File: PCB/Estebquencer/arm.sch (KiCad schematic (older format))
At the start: 1 part

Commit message: se cablearon los módulos al ARM, se añadió el conector JTAG (SWD)
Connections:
- net labels added: DAC_#Sync, DAC_Din, DAC_Sclk, DISP_CHAR0, DISP_CHAR1, DISP_CHAR2, DISP_CHAR3, DISP_EN, DISP_SCK, DISP_SER, SWCLK, SWDIO, encoder_L, encoder_R, encoder_click
- wire segments 14 -> 31
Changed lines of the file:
@@
 Connection ~ 5850 1650
 $Sheet
-S 1200 6500 1000 500
+S 1700 6500 500  500
 U 5875F97F
 F0 "JTAG" 197
 F1 "JTAG.sch" 60
+F2 "SWDIO" I R 2200 6700 60
+F3 "SWCLK" I R 2200 6800 60
 $EndSheet
 Text HLabel 2900 4100 0    60   Input ~ 0
@@
 Wire Wire Line
 	2900 4100 3050 4100
+Text GLabel 9050 4800 2    60   Input ~ 0
+SWDIO
+Text GLabel 9050 4900 2    60   Input ~ 0
+SWCLK
+Wire Wire Line
+	9050 4900 8850 4900
+Wire Wire Line
+	8850 4800 9050 4800
+Text GLabel 2300 6700 2    60   Input ~ 0
+SWDIO
+Text GLabel 2300 6800 2    60   Input ~ 0
+SWCLK
+Wire Wire Line
+	2200 6800 2300 6800
+Wire Wire Line
+	2300 6700 2200 6700
+Text HLabel 2900 3100 0    60   Input ~ 0
+encoder_L
+Text HLabel 2900 3200 0    60   Input ~ 0
+encoder_R
+Text HLabel 2900 3300 0    60   Input ~ 0
+encoder_click
+Wire Wire Line
+	2900 3100 3050 3100
+Wire Wire Line
+	3050 3200 2900 3200
+Wire Wire Line
+	2900 3300 3050 3300
+Text HLabel 2900 4000 0    60   Input ~ 0
+DAC_Din
+Text HLabel 2900 3800 0    60   Input ~ 0
+DAC_Sclk
+Text HLabel 2900 3900 0    60   Input ~ 0
+DAC_#Sync
+Wire Wire Line
+	2900 3800 3050 3800
+Wire Wire Line
+	2900 3900 3050 3900
+Wire Wire Line
+	3050 4000 2900 4000
+Text HLabel 2900 4800 0    60   Input ~ 0
+DISP_SCK
+Text HLabel 2900 5000 0    60   Input ~ 0
+DISP_SER
+Text HLabel 2900 4700 0    60   Input ~ 0
+DISP_EN
+Wire Wire Line
+	2900 4700 3050 4700
+Wire Wire Line
+	2900 4800 3050 4800
+Wire Wire Line
+	2900 5000 3050 5000
+Text HLabel 2900 4300 0    60   Input ~ 0
+DISP_CHAR0
+Text HLabel 2900 4400 0    60   Input ~ 0
+DISP_CHAR1
+Text HLabel 2900 4500 0    60   Input ~ 0
+DISP_CHAR2
+Text HLabel 2900 4600 0    60   Input ~ 0
+DISP_CHAR3
+Wire Wire Line
+	2900 4600 3050 4600
+Wire Wire Line
+	3050 4500 2900 4500
+Wire Wire Line
+	2900 4400 3050 4400
+Wire Wire Line
+	3050 4300 2900 4300
 $EndSCHEMATC

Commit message: Añadido proyecto ST, configuración superficial de todos los periféricos, falta crear los threads en FreeRTOS
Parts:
- U?: symbol STM32F103C8T6 -> libreria_proyecto:STM32F103C8T6
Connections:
- net labels added: Btn_C1, Btn_C2, Btn_C3, Btn_C4, Btn_C5, Btn_C6, Btn_C7, Btn_R1, Btn_R2, Btn_R3, CLK_OUT_1, CLK_OUT_2, CLK_in_1, CLK_in_2, DAC1_CS, DAC2_CS, DAC_MISO, DAC_MOSI, DAC_SCK, Debug_Rx, Debug_Tx, LED_R1, LED_R2, LED_R3, LED_R4, LED_R5, LED_R6, LED_R7, USB_D+, USB_D-
- net labels removed: DAC_#Sync, DAC_Din, DAC_Sclk, DISP_CHAR0, DISP_CHAR1, DISP_CHAR2, DISP_CHAR3, DISP_EN, DISP_SCK, DISP_SER, MIDI_RX, MIDI_TX, encoder_L, encoder_R, encoder_click
- wire segments 31 -> 52

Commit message: acabado módulo ARM
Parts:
- added C? (x4): 100nF, symbol Device:C_Small
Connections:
- net GNDREF is gone; now on net GND: U?.23 (VSS), U?.35 (VSS), U?.47 (VSS)
- net +3V3: now also U?.9 (VDDA), C?.1, C?.1, C?.1, C?.1
- net GND: now reaches U?.8 (VSSA)
- net GND: now also C?.2, C?.2, C?.2, C?.2
- no-connect marks 0 -> 3
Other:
- note added: "To ARM"
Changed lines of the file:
@@
 Wire Wire Line
 	1400 6300 1450 6300
-$Comp
-L power:GNDREF #PWR?
-U 1 1 5875F33E
-P 6100 5850
-F 0 "#PWR?" H 6100 5600 50  0001 C CNN
-F 1 "GNDREF" H 6100 5700 50  0000 C CNN
-F 2 "" H 6100 5850 50  0000 C CNN
-F 3 "" H 6100 5850 50  0000 C CNN
-	1    6100 5850
-	1    0    0    -1
-$EndComp
 Wire Wire Line
 	6100 5850 6100 5400
@@
 Wire Wire Line
 	3300 4800 3400 4800
+Wire Wire Line
+	9200 4900 9400 4900
+NoConn ~ 9400 4900
+Wire Wire Line
+	9400 3500 9200 3500
+Wire Wire Line
+	9200 3400 9400 3400
+NoConn ~ 9400 3400
+NoConn ~ 9400 3500
+Connection ~ 6300 5400
+Wire Wire Line
+	6400 5300 6400 5400
+Wire Wire Line
+	6300 5400 6400 5400
+Wire Wire Line
+	6400 1700 6400 1550
+Wire Wire Line
+	6400 1550 6300 1550
+Connection ~ 6300 1550
+$Comp
+L Device:C_Small C?
+U 1 1 5E3C7F8F
+P 3950 7000
+F 0 "C?" H 4000 6850 50  0000 L CNN
+F 1 "100nF" V 4050 6900 50  0000 L CNN
+F 2 "" H 3950 7000 50  0001 C CNN
+F 3 "~" H 3950 7000 50  0001 C CNN
+	1    3950 7000
+	1    0    0    -1
+$EndComp
+$Comp
+L Device:C_Small C?
+U 1 1 5E3C867B
+P 3700 7000
+F 0 "C?" H 3750 6850 50  0000 L CNN
+F 1 "100nF" V 3800 6900 50  0000 L CNN
+F 2 "" H 3700 7000 50  0001 C CNN
+F 3 "~" H 3700 7000 50  0001 C CNN
+	1    3700 7000
+	1    0    0    -1
+$EndComp
+$Comp
+L power:GND #PWR?
+U 1 1 5E3C872F
+P 6100 5850
+F 0 "#PWR?" H 6100 5600 50  0001 C CNN
+F 1 "GND" H 6105 5677 50  0000 C CNN
+F 2 "" H 6100 5850 50  0001 C CNN
+F 3 "" H 6100 5850 50  0001 C CNN
+	1    6100 5850
+	1    0    0    -1
+$EndComp
+$Comp
+L power:GND #PWR?
+U 1 1 5E3CBE0D
+P 3950 7200
+F 0 "#PWR?" H 3950 6950 50  0001 C CNN
+F 1 "GND" H 3955 7027 50  0000 C CNN
+F 2 "" H 3950 7200 50  0001 C CNN
+F 3 "" H 3950 7200 50  0001 C CNN
+	1    3950 7200
+	1    0    0    -1
+$EndComp
+$Comp
+L power:+3.3V #PWR?
+U 1 1 5E3CBE42
+P 3950 6800
+F 0 "#PWR?" H 3950 6650 50  0001 C CNN
+F 1 "+3.3V" H 3950 6940 50  0000 C CNN
+F 2 "" H 3950 6800 50  0000 C CNN
+F 3 "" H 3950 6800 50  0000 C CNN
+	1    3950 6800
+	1    0    0    -1
+$EndComp
+$Comp
+L power:+3.3V #PWR?
+U 1 1 5E3CBE88
+P 3700 6800
+F 0 "#PWR?" H 3700 6650 50  0001 C CNN
+F 1 "+3.3V" H 3700 6940 50  0000 C CNN
+F 2 "" H 3700 6800 50  0000 C CNN
+F 3 "" H 3700 6800 50  0000 C CNN
+	1    3700 6800
+	1    0    0    -1
+$EndComp
+$Comp
+L power:GND #PWR?
+U 1 1 5E3CBEC9
+P 3700 7200
+F 0 "#PWR?" H 3700 6950 50  0001 C CNN
+F 1 "GND" H 3705 7027 50  0000 C CNN
+F 2 "" H 3700 7200 50  0001 C CNN
+F 3 "" H 3700 7200 50  0001 C CNN
+	1    3700 7200
+	1    0    0    -1
+$EndComp
+Wire Wire Line
+	3700 7200 3700 7100
+Wire Wire Line
+	3700 6900 3700 6800
+Wire Wire Line
+	3950 6800 3950 6900
+Wire Wire Line
+	3950 7100 3950 7200
+$Comp
+L Device:C_Small C?
+U 1 1 5E3D0FF3
+P 4700 7000
+F 0 "C?" H 4750 6850 50  0000 L CNN
+F 1 "100nF" V 4800 6900 50  0000 L CNN
+F 2 "" H 4700 7000 50  0001 C CNN
+F 3 "~" H 4700 7000 50  0001 C CNN
+	1    4700 7000
+	1    0    0    -1
+$EndComp
+$Comp
+L Device:C_Small C?
+U 1 1 5E3D0FF9
+P 4450 7000
+F 0 "C?" H 4500 6850 50  0000 L CNN
+F 1 "100nF" V 4550 6900 50  0000 L CNN
+F 2 "" H 4450 7000 50  0001 C CNN
+F 3 "~" H 4450 7000 50  0001 C CNN
+	1    4450 7000
+	1    0    0    -1
+$EndComp
+$Comp
+L power:GND #PWR?
+U 1 1 5E3D0FFF
+P 4700 7200
+F 0 "#PWR?" H 4700 6950 50  0001 C CNN
+F 1 "GND" H 4705 7027 50  0000 C CNN
+F 2 "" H 4700 7200 50  0001 C CNN
+F 3 "" H 4700 7200 50  0001 C CNN
+	1    4700 7200
+	1    0    0    -1
+$EndComp
+$Comp
+L power:+3.3V #PWR?
+U 1 1 5E3D1005
+P 4700 6800
+F 0 "#PWR?" H 4700 6650 50  0001 C CNN
+F 1 "+3.3V" H 4700 6940 50  0000 C CNN
+F 2 "" H 4700 6800 50  0000 C CNN
+F 3 "" H 4700 6800 50  0000 C CNN
+	1    4700 6800
+	1    0    0    -1
+$EndComp
+$Comp
+L power:+3.3V #PWR?
+U 1 1 5E3D100B
+P 4450 6800
+F 0 "#PWR?" H 4450 6650 50  0001 C CNN
+F 1 "+3.3V" H 4450 6940 50  0000 C CNN
+F 2 "" H 4450 6800 50  0000 C CNN
+F 3 "" H 4450 6800 50  0000 C CNN
+	1    4450 6800
+	1    0    0    -1
+$EndComp
+$Comp
+L power:GND #PWR?
+U 1 1 5E3D1011
+P 4450 7200
+F 0 "#PWR?" H 4450 6950 50  0001 C CNN
+F 1 "GND" H 4455 7027 50  0000 C CNN
+F 2 "" H 4450 7200 50  0001 C CNN
+F 3 "" H 4450 7200 50  0001 C CNN
+	1    4450 7200
+	1    0    0    -1
+$EndComp
+Wire Wire Line
+	4450 7200 4450 7100
+Wire Wire Line
+	4450 6900 4450 6800
+Wire Wire Line
+	4700 6800 4700 6900
+Wire Wire Line
+	4700 7100 4700 7200
+Text Notes 3700 6500 0    60   ~ 0
+To ARM
+Text Notes 4450 6500 0    60   ~ 0
+To ARM
 $EndSCHEMATC

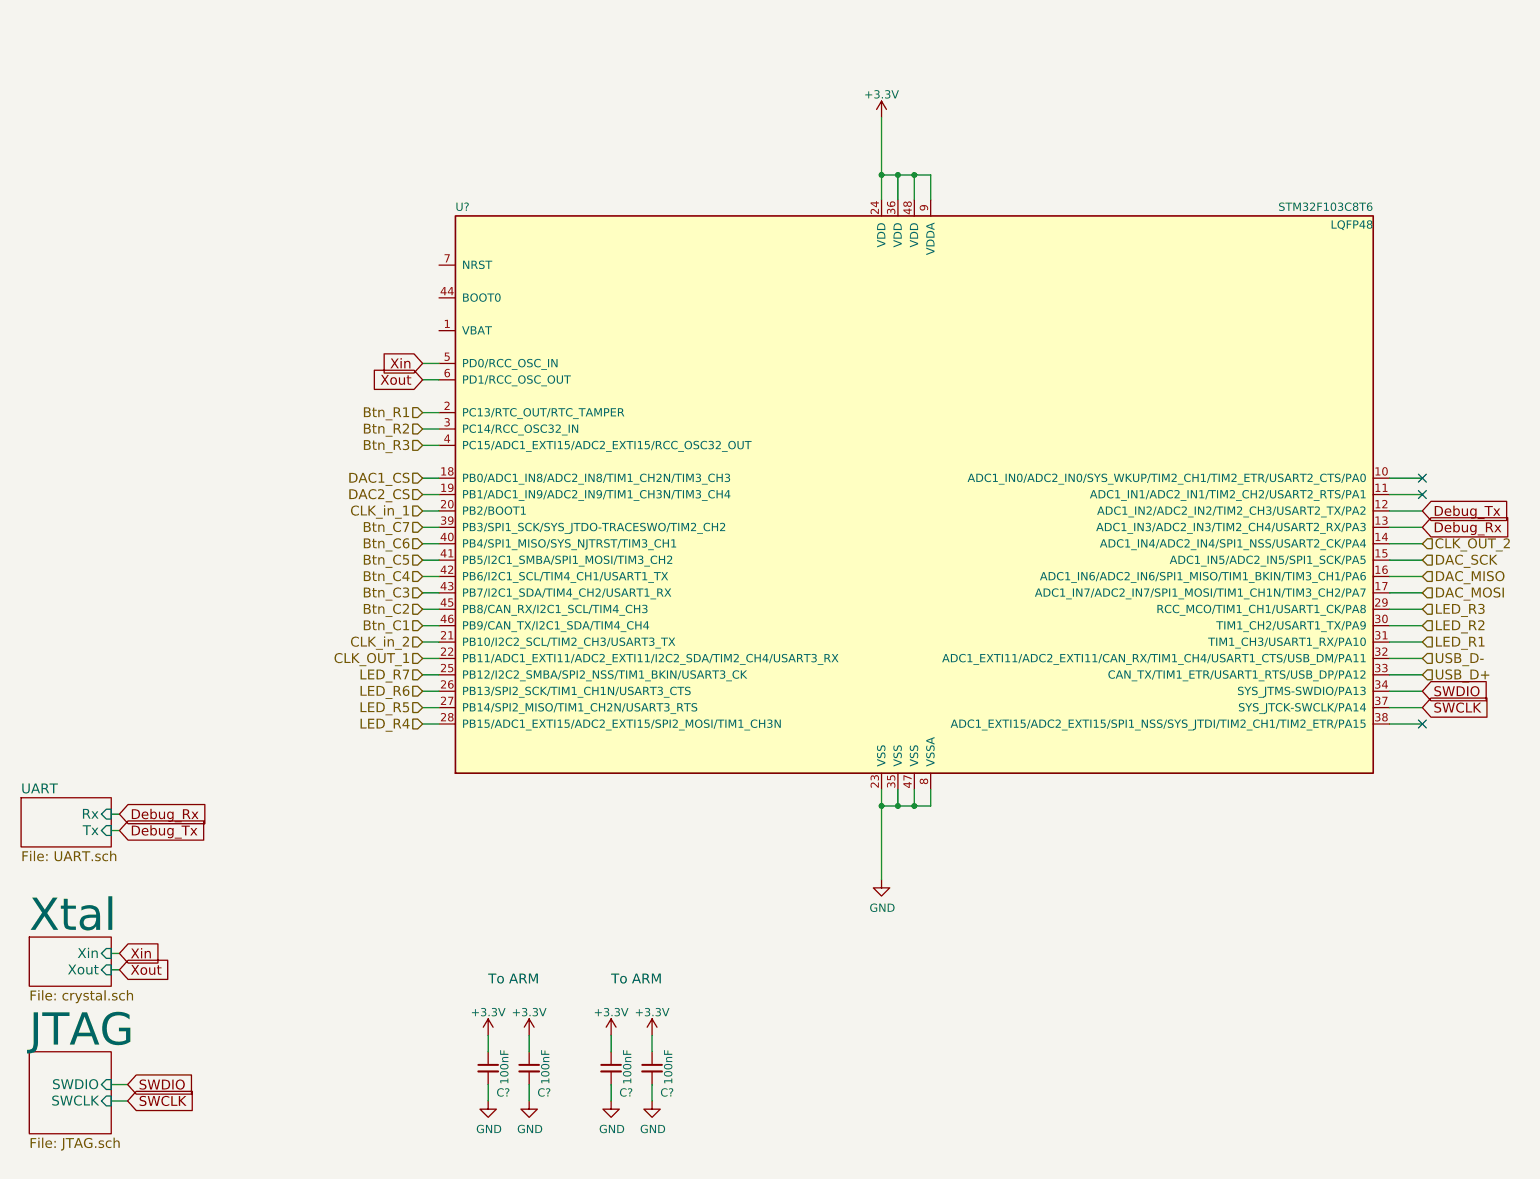
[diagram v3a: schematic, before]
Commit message: arreglado boot0, boot1 y reset
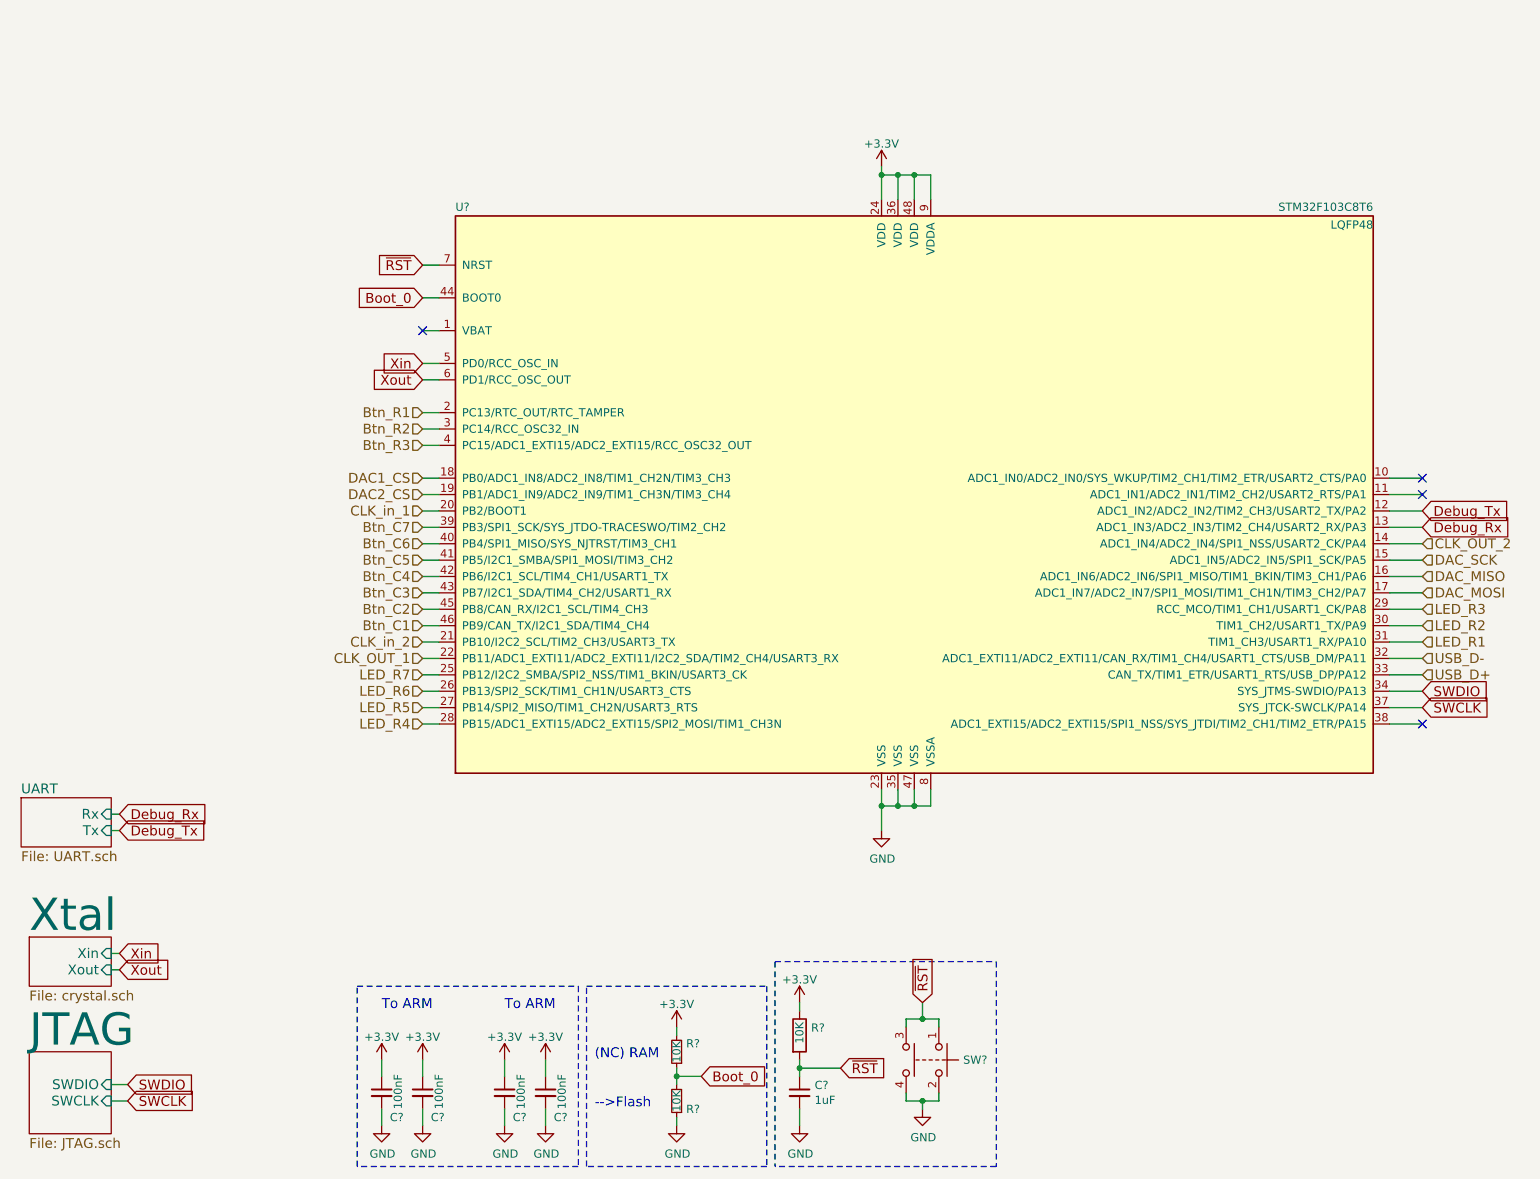
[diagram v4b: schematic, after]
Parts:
- added C?: 1uF, symbol Device:C_Small
- added R? (x2): 10K, symbol Device:R_Small
- added R?: 10K, symbol Device:R
- added SW?: SW_Push_Dual, symbol Switch:SW_Push_Dual
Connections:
- net +3V3: now also R?.1, R?.2
- net GND: now also C?.2, R?.1, SW?.2, SW?.4
- net Boot_0: now reaches U?.44 (BOOT0)
- net Boot_0: now also R?.1, R?.2
- net ~RST~: now reaches U?.7 (NRST)
- net ~RST~: now also C?.1, R?.2, SW?.1, SW?.3
- no-connect marks 3 -> 4
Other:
- note added: "(NC) RAM"
- note added: "-->Flash"
- moved on the sheet: C?
